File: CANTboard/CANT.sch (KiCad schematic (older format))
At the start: 49 parts, among them J1 Screw_Terminal_01x04, J2 Conn_02x08_Odd_Even, P1 SWD, P3 USB, SW1 SW_SPST, U1 STM32H743VITx, U2 MCP2558FD-xSN, U3 LD1117S33TR, U4 74LVC1G66, U5 74LVC1G66, U6 MCP2558FD-xSN, U7 USBLC6-2SC6, Y1 Crystal

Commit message: Finished layout, ordered first set of prototype boards
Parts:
- added C12, C13: 2.2uF, Capacitor_SMD:C_0805_2012Metric, symbol Device:C
- added C2, C8: 100nF, Capacitor_SMD:C_0805_2012Metric, symbol pspice:C
- added J2: Screw_Terminal_01x02, TerminalBlock_Phoenix:TerminalBlock_Phoenix_PT-1,5-2-3.5-H_1x02_P3.50mm_Horizontal, symbol Connector:Screw_Terminal_01x02
- added R4, R5: 4.7K, Resistor_SMD:R_0805_2012Metric, symbol pspice:R
- added R7, R8: 47, Resistor_SMD:R_0805_2012Metric, symbol pspice:R
- added U2: SN74LVC1G14DBV, Package_TO_SOT_SMD:SOT-23-5, symbol 74xGxx:SN74LVC1G14DBV
- added U3: ST485EBDR, Package_SO:SOIC-8_3.9x4.9mm_P1.27mm, symbol Interface_UART:ST485EBDR
- renumbered C13 to C10, C8 to C11, C9 to C14, C10 to C15, C18 to C16, C19 to C17, C20 to C18, C14 to C19, C15 to C20, C5 to C21, C6 to C22, C16 to C23, C17 to C24, C2 to C3, C3 to C4, C4 to C5, C11 to C6, C12 to C9, J2 to J1, J1 to J3, JP3 to JP1, JP1 to JP3, P3 to P1, P1 to P2, R3 to R1, R7 to R10, R1 to R11, R5 to R12, R2 to R13, R4 to R2, R8 to R3, R9 to R6, R6 to R9, U7 to U1, U3 to U4, U1 to U5, U2 to U6, U5 to U7, U6 to U8, U4 to U9
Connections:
- net GND: now also C12.2, C13.1, C2.1, C8.2, R4.2, U2.3 (GND), U3.2 (~RE), U3.4 (DI), U3.5 (GND)
- net VBUS: now also R5.1
- net VCC: now also C2.2, C8.1, U2.5 (VCC), U3.8 (VCC)
- net J1708_TX: now reaches U5.22 (PA0)
- net J1708_TX: now also U2.2
- net J1708_RX: now reaches U5.23 (PA1)
- net J1708_RX: now also U3.1 (RO)
- new net: U2.4, U3.3 (DE)
- new net: C13.2, R5.2, R8.1, U3.6 (A)
- new net: C12.1, R4.1, R7.1, U3.7 (B)
- new net: J2.1 (Pin_1), R8.2
- new net: J2.2 (Pin_2), R7.2
- no-connect marks 63 -> 61
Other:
- note added: "J1708"
- moved on the sheet: C1, C10, C11, C3, C4, C5, C6, C7, C9, D1, D2, D3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

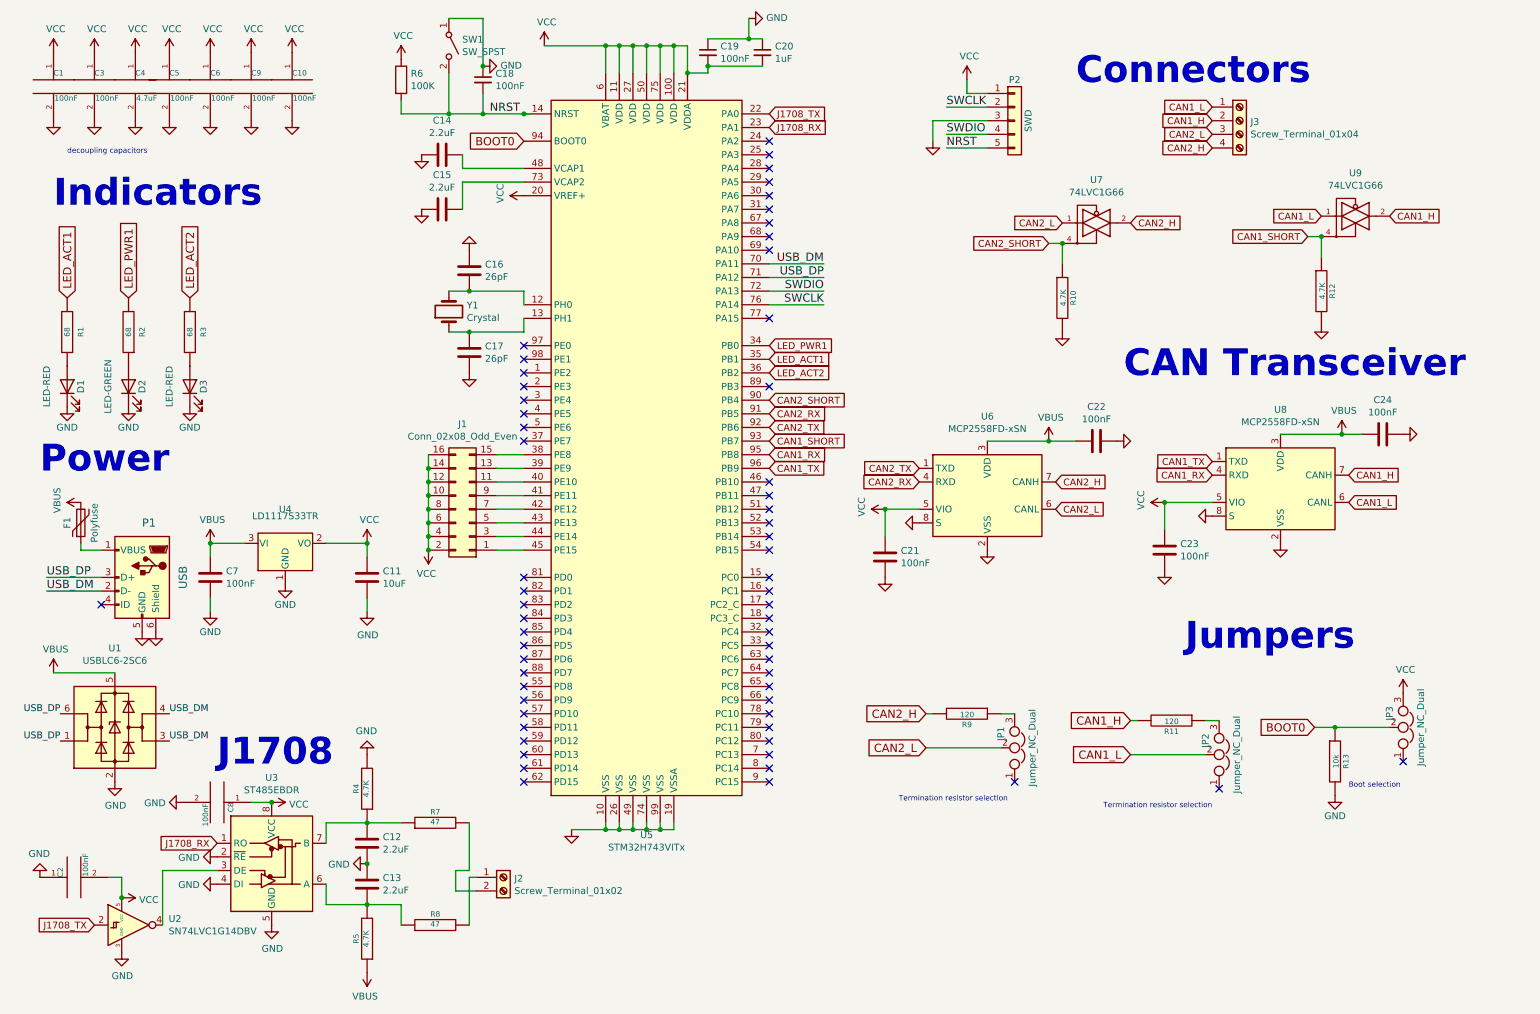
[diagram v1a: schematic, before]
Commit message: Switched to USB-C, in process of switching to USB-HS
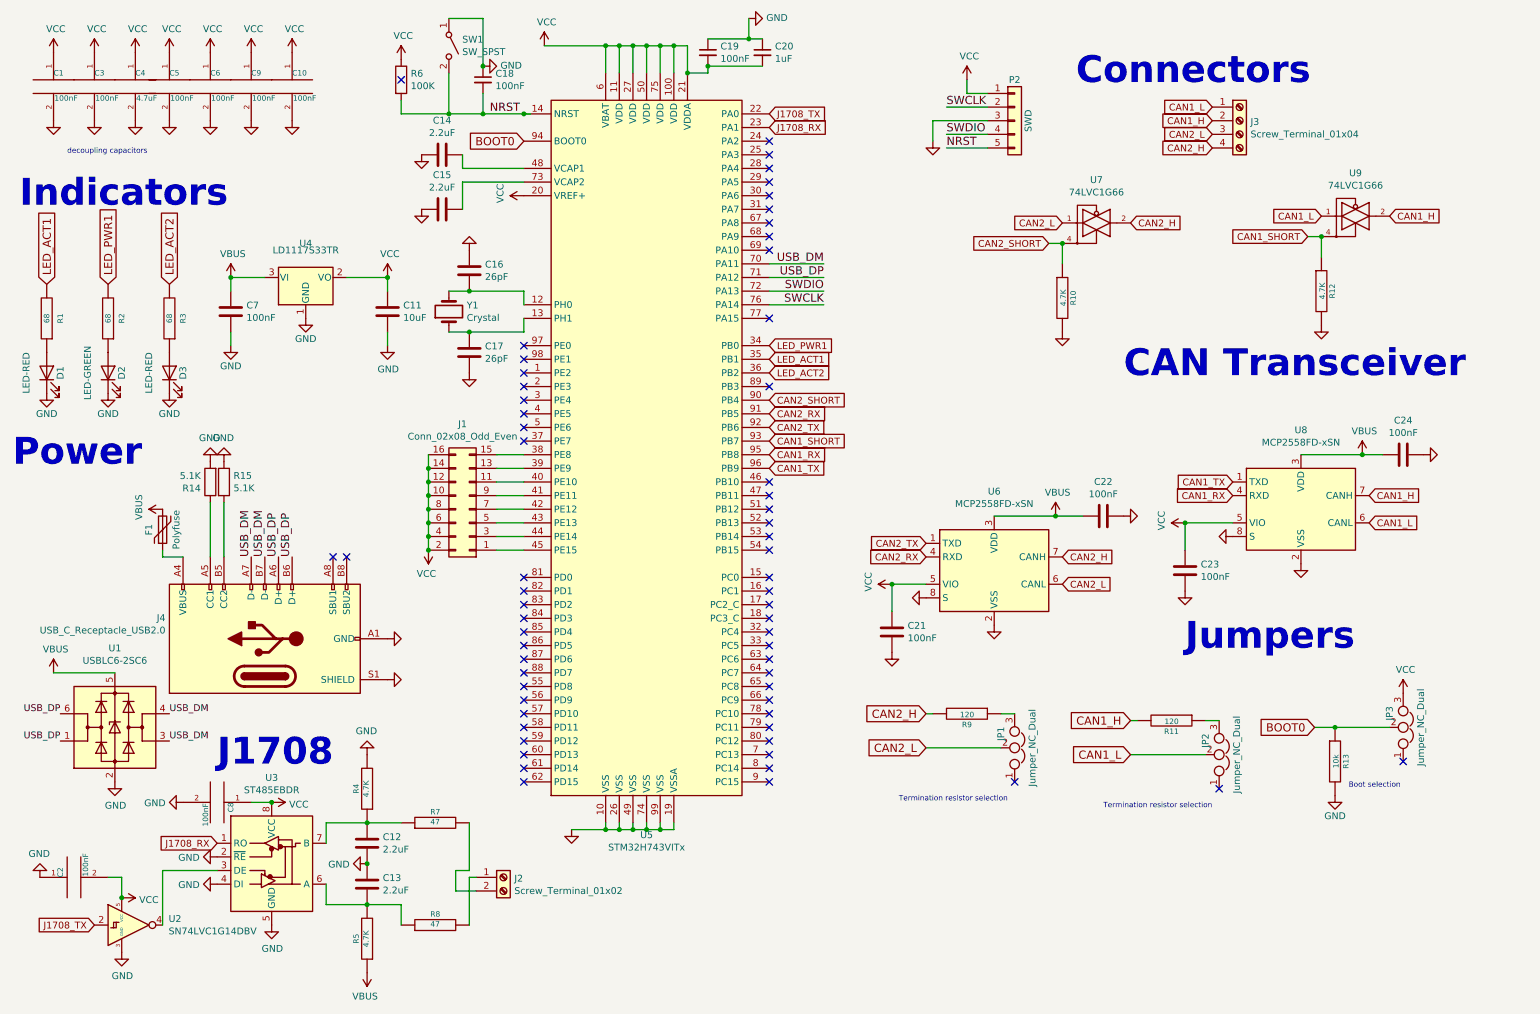
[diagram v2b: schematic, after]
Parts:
- removed P1: USB, Connector_USB:USB_Micro-B_Molex_47346-0001, symbol CANT-rescue:USB_B_Micro-Connector
- added J4: USB_C_Receptacle_USB2.0, Connector_USB:USB_C_Receptacle_GCT_USB4085, symbol Connector:USB_C_Receptacle_USB2.0
- added R14, R15: 5.1K, Resistor_SMD:R_0603_1608Metric, symbol Device:R
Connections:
- net GND: now also J4.A1 (GND), J4.A12 (GND), J4.B1 (GND), J4.B12 (GND), J4.S1 (SHIELD), R14.2, R15.1
- net USB_DM: now also J4.A7 (D-), J4.B7 (D-)
- net USB_DP: now also J4.A6 (D+), J4.B6 (D+)
- net at F1.1: now also J4.A4 (VBUS), J4.A9 (VBUS), J4.B4 (VBUS), J4.B9 (VBUS)
- new net: J4.A5 (CC1), R14.1
- new net: J4.B5 (CC2), R15.2
- no-connect marks 61 -> 63
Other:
- moved on the sheet: C11, C21, C22, C23, C24, C7, D1, D2, D3, F1, R1, R2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

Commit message: Re-design for 480mbps USB-C. Schematic split into multiple sheets, connections made, ERC passes, footprints assigned.
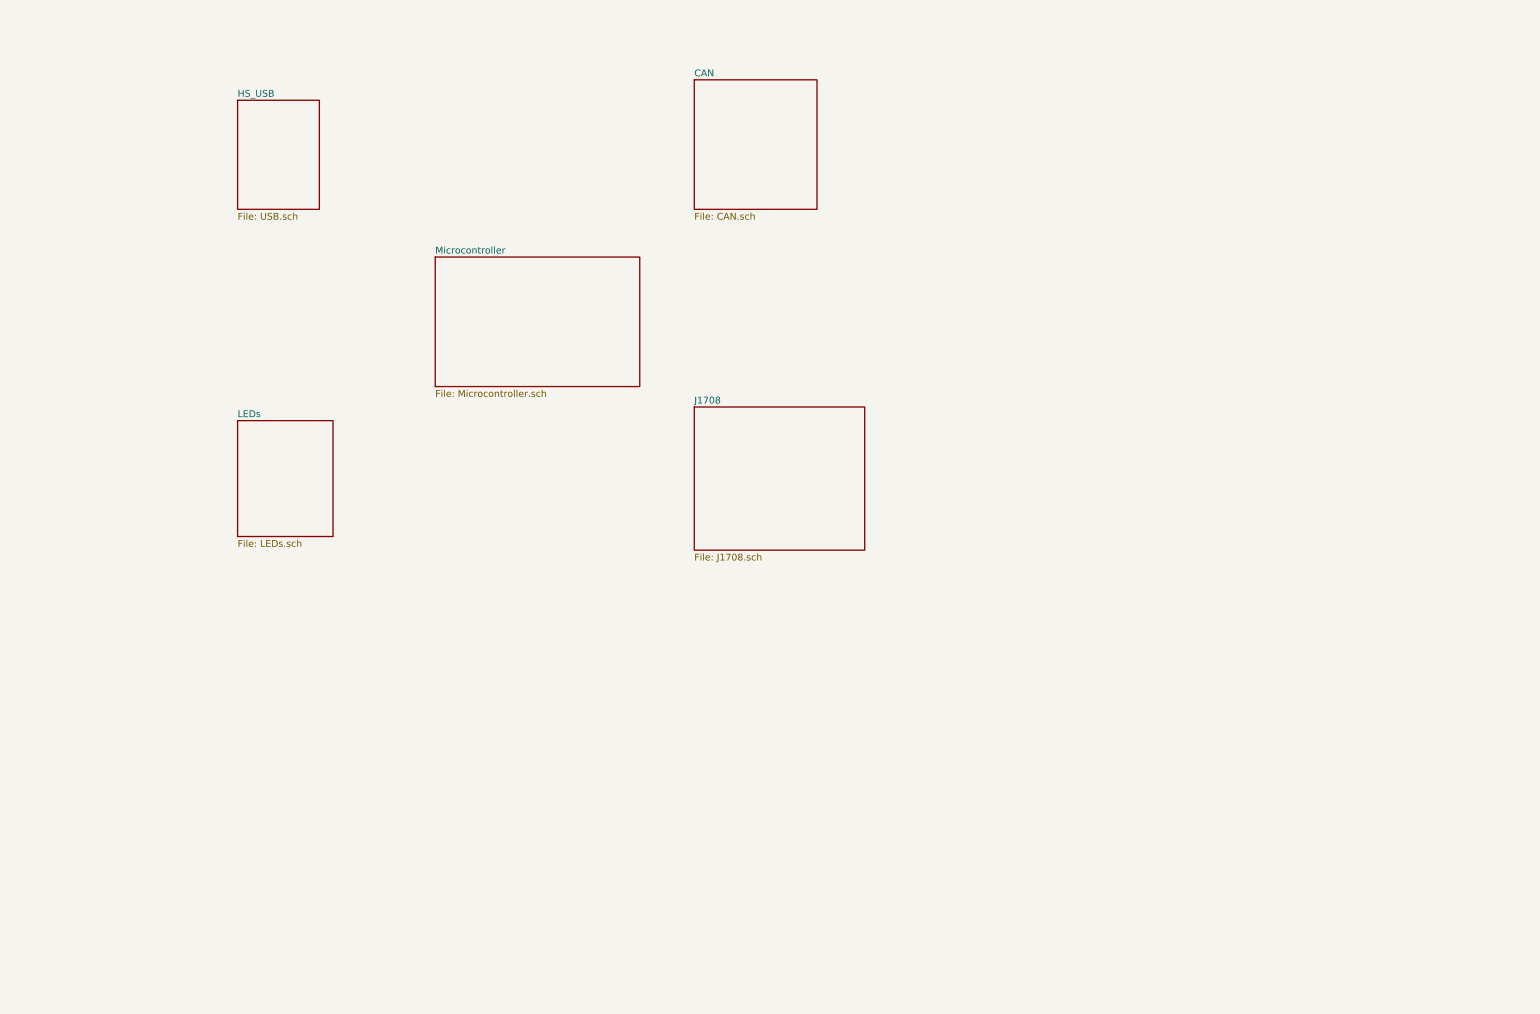
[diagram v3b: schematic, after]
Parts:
- removed C1, C10, C2, C3, C5, C6, C8, C9: 100nF, Capacitor_SMD:C_0805_2012Metric, symbol pspice:C
- removed C11: 10uF, Capacitor_SMD:C_0805_2012Metric, symbol Device:C
- removed C12, C13, C14, C15: 2.2uF, Capacitor_SMD:C_0805_2012Metric, symbol Device:C
- removed C16, C17: 26pF, Capacitor_SMD:C_0805_2012Metric, symbol Device:C
- removed C18, C19: 100nF, Capacitor_SMD:C_0805_2012Metric, symbol Device:C_Small
- removed C20: 1uF, Capacitor_SMD:C_0805_2012Metric, symbol Device:C_Small
- removed C21, C22, C23, C24, C7: 100nF, Capacitor_SMD:C_0805_2012Metric, symbol Device:C
- removed C4: 4.7uF, Capacitor_SMD:C_0805_2012Metric, symbol pspice:C
- removed D1, D3: LED-RED, LED_SMD:LED_0805_2012Metric, symbol Device:LED
- removed D2: LED-GREEN, LED_SMD:LED_0805_2012Metric, symbol Device:LED
- removed F1: Polyfuse, Capacitor_SMD:C_0805_2012Metric, symbol Device:Polyfuse
- removed J1: Conn_02x08_Odd_Even, Connector_PinHeader_2.54mm:PinHeader_2x08_P2.54mm_Vertical, symbol Connector_Generic:Conn_02x08_Odd_Even
- removed J2: Screw_Terminal_01x02, TerminalBlock_Phoenix:TerminalBlock_Phoenix_PT-1,5-2-3.5-H_1x02_P3.50mm_Horizontal, symbol Connector:Screw_Terminal_01x02
- removed J3: Screw_Terminal_01x04, TerminalBlock_Phoenix:TerminalBlock_Phoenix_PT-1,5-4-3.5-H_1x04_P3.50mm_Horizontal, symbol Connector:Screw_Terminal_01x04
- removed J4: USB_C_Receptacle_USB2.0, Connector_USB:USB_C_Receptacle_GCT_USB4085, symbol Connector:USB_C_Receptacle_USB2.0
- removed JP1, JP2, JP3: Jumper_NC_Dual, Connector_PinHeader_2.54mm:PinHeader_1x03_P2.54mm_Vertical, symbol Device:Jumper_NC_Dual
- removed P2: SWD, Connector_PinHeader_2.54mm:PinHeader_1x05_P2.54mm_Vertical, symbol Connector_Generic:Conn_01x05
- removed R1, R2, R3: 68, Resistor_SMD:R_0805_2012Metric, symbol pspice:R
- removed R10, R12, R4, R5: 4.7K, Resistor_SMD:R_0805_2012Metric, symbol pspice:R
- removed R11, R9: 120, Resistor_SMD:R_0805_2012Metric, symbol pspice:R
- removed R13: 10k, Resistor_SMD:R_0805_2012Metric, symbol pspice:R
- removed R14, R15: 5.1K, Resistor_SMD:R_0603_1608Metric, symbol Device:R
- removed R6: 100K, Resistor_SMD:R_0805_2012Metric, symbol Device:R
- removed R7, R8: 47, Resistor_SMD:R_0805_2012Metric, symbol pspice:R
- removed SW1: SW_SPST, Button_Switch_SMD:SW_SPST_PTS645, symbol Switch:SW_SPST
- removed U1: USBLC6-2SC6, Package_TO_SOT_SMD:SOT-23-6, symbol Power_Protection:USBLC6-2SC6
- removed U2: SN74LVC1G14DBV, Package_TO_SOT_SMD:SOT-23-5, symbol 74xGxx:SN74LVC1G14DBV
- removed U3: ST485EBDR, Package_SO:SOIC-8_3.9x4.9mm_P1.27mm, symbol Interface_UART:ST485EBDR
- removed U4: LD1117S33TR, Package_TO_SOT_SMD:SOT-223, symbol Regulator_Linear:LD1117S33TR_SOT223
- removed U5: STM32H743VITx, Package_QFP:LQFP-100_14x14mm_P0.5mm, symbol MCU_ST_STM32H7:STM32H743VITx
- removed U6, U8: MCP2558FD-xSN, Package_SO:SOIC-8_3.9x4.9mm_P1.27mm, symbol Interface_CAN_LIN:MCP2558FD-xSN
- removed U7, U9: 74LVC1G66, Package_TO_SOT_SMD:SOT-353_SC-70-5_Handsoldering, symbol CANT-rescue:74LVC1G66-74xGxx
- removed Y1: Crystal, Crystal:Crystal_SMD_HC49-SD, symbol Device:Crystal
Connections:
- no-connect marks 63 -> 0
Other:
- note removed: "Boot selection"
- note removed: "CAN Transceiver"
- note removed: "Connectors"
- note removed: "Indicators"
- note removed: "J1708"
- note removed: "Jumpers"
- note removed: "Power"
- note removed: "Termination resistor selection"
- note removed: "decoupling capacitors"
